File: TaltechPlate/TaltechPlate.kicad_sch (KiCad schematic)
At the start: 8 parts, among them J1 Conn_01x02, J2 Conn_01x04

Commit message: Updated new parts MFN and MPN as well as title block
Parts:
- J1: MPN (none) -> XT-30
- J2: MFN (none) -> JST Commercial; MPN (none) -> B4B-PH-K-S(LF)(SN); Mouser_PN (none) -> 306-B4BPHKSLFSNPP
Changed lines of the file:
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@@
+			)
+		)
+		(property "S1PN" ""
+			(at 171.45 49.53 0)
+			(effects
+				(font
+					(size 1.27 1.27)
+				)
+				(hide yes)
+			)
+		)
+		(property "S1PL" ""
+			(at 171.45 49.53 0)
+			(effects
+				(font
+					(size 1.27 1.27)
+				)
+				(hide yes)
+			)
+		)
+		(property "S1SN" ""
+			(at 171.45 49.53 0)
+			(effects
+				(font
+					(size 1.27 1.27)
+				)
+				(hide yes)
+			)
+		)
+		(property "MFN" "JST Commercial "
+			(at 171.45 49.53 0)
+			(effects
+				(font
+					(size 1.27 1.27)
+				)
+				(hide yes)
+			)
+		)
+		(property "MPN" " B4B-PH-K-S(LF)(SN) "
+			(at 171.45 49.53 0)
+			(effects
+				(font
+					(size 1.27 1.27)
+				)
+				(hide yes)
+			)
+		)
+		(property "Mouser_PN" " 306-B4BPHKSLFSNPP "
+			(at 171.45 49.53 0)
+			(effects
+				(font
+					(size 1.27 1.27)
+				)
+				(hide yes)
 			)
 		)
@@
 			(at 168.91 88.9 0)
 			(effects
+				(font
+					(size 1.27 1.27)
+				)
+				(hide yes)
+			)
+		)
+		(property "S1PN" ""
+			(at 168.91 88.9 0)
+			(effects
+				(font
+					(size 1.27 1.27)
+				)
+				(hide yes)
+			)
+		)
+		(property "S1PL" ""
+			(at 168.91 88.9 0)
+			(effects
+				(font
+					(size 1.27 1.27)
+				)
+				(hide yes)
+			)
+		)
+		(property "S1SN" ""
+			(at 168.91 88.9 0)
+			(effects
+				(font
+					(size 1.27 1.27)
+				)
+				(hide yes)
+			)
+		)
+		(property "MFN" ""
+			(at 168.91 88.9 0)
+			(effects
+				(font
+					(size 1.27 1.27)
+				)
+				(hide yes)
+			)
+		)
+		(property "MPN" "XT-30"
+			(at 168.91 88.9 0)
+			(effects

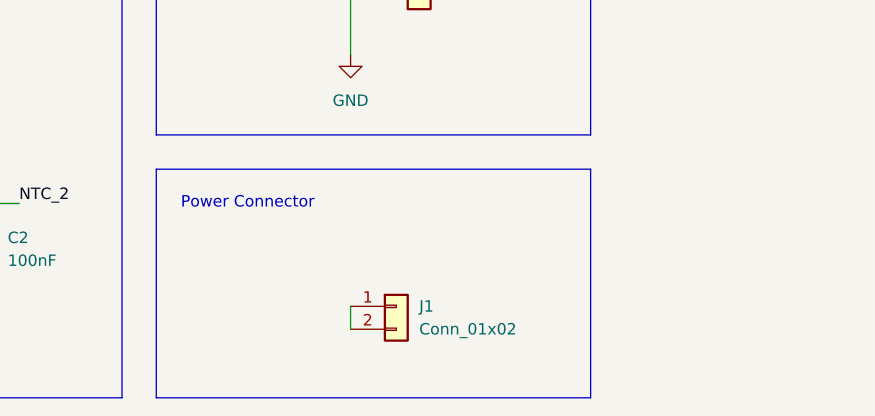
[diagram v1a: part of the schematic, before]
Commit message: Mounting holes and longer trace on plate
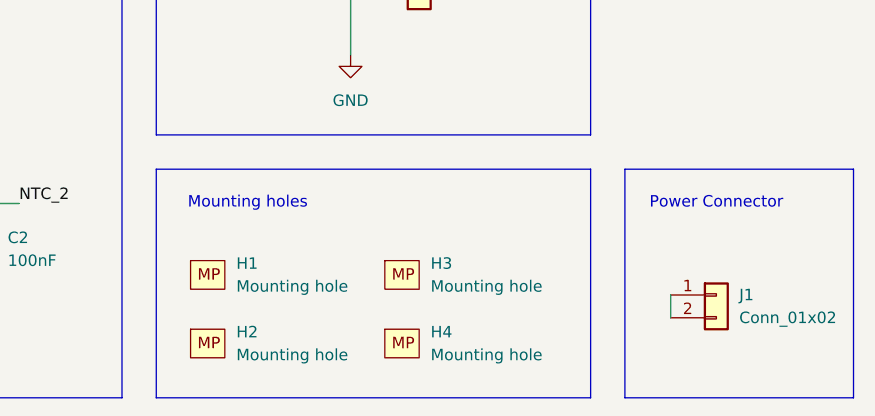
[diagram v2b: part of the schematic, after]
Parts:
- added H1, H2, H3, H4: Mounting hole, MountingHole:MountingHole_3.2mm_M3_DIN965, symbol AA:Mechanical Part
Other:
- note added: "Mounting holes"
- moved on the sheet: J1
